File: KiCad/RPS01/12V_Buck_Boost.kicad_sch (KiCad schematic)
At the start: 0 parts

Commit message: Updfates
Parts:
- added C(STBYMD)1, Css1: 0.001u, Capacitor_SMD:C_1206_3216Metric, symbol Device:C
- added C(lowESR)1: 4.7u, Mechatronic Footprints:LOWESRCAPMP7.6X4.3_3.1N_KEM, symbol Device:C
- added Ca(SW1)1, Cb(SW2)1: 0.22u, Capacitor_SMD:C_1206_3216Metric, symbol Device:C
- added Cb(out)1: 330u, Mechatronic Footprints:LargeCAPSCAPPRD350W60D800H1200, symbol Device:C_Polarized
- added Cc(out)1: 47u, Capacitor_SMD:C_1206_3216Metric, symbol Device:C
- added Cin(b)1: 270u, Mechatronic Footprints:LargeCAPSCAPPRD350W60D800H1200, symbol Device:C
- added Cin(c)1: 10u, Capacitor_SMD:C_1206_3216Metric, symbol Device:C
- added Cout(filter)1: 330u, Mechatronic Footprints:LargeCAPSCAPPRD350W60D800H1200, symbol Device:C
- added Cs1: 100p, Capacitor_SMD:C_1206_3216Metric, symbol Device:C
- added Cth1: 10000p, Capacitor_SMD:C_1206_3216Metric, symbol Device:C
- added Cthp1: 47p, Capacitor_SMD:C_1206_3216Metric, symbol Device:C
- added D(Zener)2: D_Zener, Mechatronic Footprints:SOD123_DIO, symbol Device:D_Zener
- added D1, D2, D4, D5: D_Schottky, Mechatronic Footprints:CR_SMA_320-340AE_DIO, symbol Device:D_Schottky
- added L1: 6.8u, Mechatronic Footprints:IND_410680_WRE, symbol Device:L
- added Q1, Q2, Q3, Q4: NMOS, Mechatronic Footprints:Q1Q2TRANS_FDMC86520L, symbol Device:Q_NMOS_DGS
- added R(pgood)1: 100k, LED_SMD:LED_1206_3216Metric, symbol Device:R
- added R4, R5: 100, Resistor_SMD:R_1206_3216Metric, symbol Device:R
- added Rb1: 4.3K, Resistor_SMD:R_1206_3216Metric, symbol Device:R
- added Rin(Run)1: 51K, Resistor_SMD:R_1206_3216Metric, symbol Device:R
- added Rs1, Rsen1: 6m, Resistor_SMD:R_2512_6332Metric, symbol Device:R
- added Rt1: 100K, Resistor_SMD:R_1206_3216Metric, symbol Device:R
- added Rth1: 124K, Resistor_SMD:R_1206_3216Metric, symbol Device:R
- added U1: LTC3780EG-TRPBF, LTC3780:SSOP-24_G_LIT, symbol LTC3780-24-SSOP:LTC3780EG-TRPBF
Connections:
- new net: C(lowESR)1.1, D4.2 (A), D5.2 (A), R(pgood)1.1, U1.19 (INTVCC)
- new net: R(pgood)1.2, U1.1 (PGOOD)
- new net: Ca(SW1)1.2, D1.2 (A), L1.2, Q3.3 (S), Q4.1 (D), U1.22 (SW1)
- new net: Q4.2 (G), U1.18 (BG1)
- new net: D2.2 (A), Q2.3 (S), Q4.3 (S), R4.1, Rs1.1, Rsen1.1
- new net: C(STBYMD)1.1, U1.12 (STBYMD)
- new net: Cb(SW2)1.2, D5.1 (K), U1.13 (BOOST2)
- new net: Q1.2 (G), U1.14 (TG2)
- new net: Cb(SW2)1.1, D2.1 (K), L1.1, Q1.3 (S), Q2.1 (D), U1.15 (SW2)
- new net: Q2.2 (G), U1.16 (BG2)
- new net: Css1.2, U1.2 (SS)
- new net: Q3.2 (G), U1.23 (TG1)
- new net: Ca(SW1)1.1, D4.1 (K), U1.24 (BOOST1)
- new net: Cs1.2, R4.2, U1.3 (SENSE+)
- new net: Cs1.1, R5.1, U1.4 (SENSE-)
- new net: Cthp1.1, Rth1.2, U1.5 (ITH)
- new net: Rb1.1, Rt1.2, U1.6 (VOSENSE)
- new net: D(Zener)2.1 (K), Rin(Run)1.2, U1.8 (RUN)
- new net: Cth1.1, Rth1.1
- new net GND: C(STBYMD)1.2, C(lowESR)1.2, Cb(out)1.2, Cc(out)1.2, Cin(b)1.2, Cin(c)1.2, Cout(filter)1.2, Css1.1, Cth1.2, Cthp1.2, D(Zener)2.2 (A), R5.2, Rb1.2, Rs1.2, Rsen1.2, U1.10 (PLLFLTR), U1.17 (PGND), U1.20 (EXTVCC), U1.7 (SGND), U1.9 (FCB)
- new net Vin: Cin(b)1.1, Cin(c)1.1, Q1.1 (D), Rin(Run)1.1, U1.21 (VIN)
- new net Vout: Cb(out)1.1, Cc(out)1.1, Cout(filter)1.1, D1.1 (K), Q3.1 (D), Rt1.1
- no-connect marks 0 -> 1

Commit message: Changed footprints on my end only
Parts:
- U1: footprint LTC3780:SSOP-24_G_LIT -> Mechatronics LTC3780:SSOP-24_G_LIT
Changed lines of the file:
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@@
       (effects (font (size 1.524 1.524)))
     )
-    (property "Footprint" "LTC3780:SSOP-24_G_LIT" (at 111.0742 89.4334 0)
+    (property "Footprint" "Mechatronics LTC3780:SSOP-24_G_LIT" (at 111.0742 89.4334 0)
       (effects (font (size 1.27 1.27) italic) hide)
     )

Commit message: All Footprints Load from Mechatronics Folder
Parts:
- U1: footprint Mechatronics LTC3780:SSOP-24_G_LIT -> Mechatronic Footprints:LTC3780_SSOP-24_G_LIT
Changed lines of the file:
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@@
       (effects (font (size 1.524 1.524)))
     )
-    (property "Footprint" "Mechatronics LTC3780:SSOP-24_G_LIT" (at 111.0742 89.4334 0)
+    (property "Footprint" "Mechatronic Footprints:LTC3780_SSOP-24_G_LIT" (at 111.0742 89.4334 0)
       (effects (font (size 1.27 1.27) italic) hide)
     )

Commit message: Deleted 12 and 5 V. 19V updated
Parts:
- removed C(STBYMD)1, Css1: 0.001u, Capacitor_SMD:C_1206_3216Metric, symbol Device:C
- removed C(lowESR)1: 4.7u, Mechatronic Footprints:LOWESRCAPMP7.6X4.3_3.1N_KEM, symbol Device:C
- removed Ca(SW1)1, Cb(SW2)1: 0.22u, Capacitor_SMD:C_1206_3216Metric, symbol Device:C
- removed Cb(out)1: 330u, Mechatronic Footprints:LargeCAPSCAPPRD350W60D800H1200, symbol Device:C_Polarized
- removed Cc(out)1: 47u, Capacitor_SMD:C_1206_3216Metric, symbol Device:C
- removed Cin(b)1: 270u, Mechatronic Footprints:LargeCAPSCAPPRD350W60D800H1200, symbol Device:C
- removed Cin(c)1: 10u, Capacitor_SMD:C_1206_3216Metric, symbol Device:C
- removed Cout(filter)1: 330u, Mechatronic Footprints:LargeCAPSCAPPRD350W60D800H1200, symbol Device:C
- removed Cs1: 100p, Capacitor_SMD:C_1206_3216Metric, symbol Device:C
- removed Cth1: 10000p, Capacitor_SMD:C_1206_3216Metric, symbol Device:C
- removed Cthp1: 47p, Capacitor_SMD:C_1206_3216Metric, symbol Device:C
- removed D(Zener)2: D_Zener, Mechatronic Footprints:SOD123_DIO, symbol Device:D_Zener
- removed D1, D2, D4, D5: D_Schottky, Mechatronic Footprints:CR_SMA_320-340AE_DIO, symbol Device:D_Schottky
- removed L1: 6.8u, Mechatronic Footprints:IND_410680_WRE, symbol Device:L
- removed Q1, Q2, Q3, Q4: NMOS, Mechatronic Footprints:Q1Q2TRANS_FDMC86520L, symbol Device:Q_NMOS_DGS
- removed R(pgood)1: 100k, LED_SMD:LED_1206_3216Metric, symbol Device:R
- removed R4, R5: 100, Resistor_SMD:R_1206_3216Metric, symbol Device:R
- removed Rb1: 4.3K, Resistor_SMD:R_1206_3216Metric, symbol Device:R
- removed Rin(Run)1: 51K, Resistor_SMD:R_1206_3216Metric, symbol Device:R
- removed Rs1, Rsen1: 6m, Resistor_SMD:R_2512_6332Metric, symbol Device:R
- removed Rt1: 100K, Resistor_SMD:R_1206_3216Metric, symbol Device:R
- removed Rth1: 124K, Resistor_SMD:R_1206_3216Metric, symbol Device:R
- removed U1: LTC3780EG-TRPBF, Mechatronic Footprints:LTC3780_SSOP-24_G_LIT, symbol LTC3780-24-SSOP:LTC3780EG-TRPBF
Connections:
- no-connect marks 1 -> 0

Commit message: Added prototype 12V and 5V boards
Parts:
- added C(STBYMD)1, Css1: 0.001u, Capacitor_SMD:C_1206_3216Metric, symbol Device:C
- added C(lowESR)1: 4.7u, Mechatronics Cesr:CAPMP7.6X4.3_3.1N_KEM, symbol Device:C
- added Ca(SW1)1, Cb(SW2)1: 0.22u, Capacitor_SMD:C_1206_3216Metric, symbol Device:C
- added Cc(out)1: 47u, Capacitor_SMD:C_1206_3216Metric, symbol Device:C
- added Cin(b)1: 270u, Mechatronic Footprints:LargeCAPSCAPPRD350W60D800H1200, symbol Device:C
- added Cin(c)1: 10u, Capacitor_SMD:C_1206_3216Metric, symbol Device:C
- added Cout_19V_EEH-ZU1V331P1: 330u, Mechatronic Footprints:LargeCAPSCAPPRD350W60D800H1200, symbol Device:C
- added Cout_b_19V_EEH-ZU1V331P1: 330u, Mechatronic Footprints:LargeCAPSCAPPRD350W60D800H1200, symbol Device:C_Polarized
- added Cs1: 100p, Capacitor_SMD:C_1206_3216Metric, symbol Device:C
- added Cth1: 10000p, Capacitor_SMD:C_1206_3216Metric, symbol Device:C
- added Cthp1: 47p, Capacitor_SMD:C_1206_3216Metric, symbol Device:C
- added D(Zener)_19V1: D_Zener_BZT52C4V7-13-F, Mechatronic Footprints:SOD123_DIO, symbol Device:D_Zener
- added D1(2)_19V1, D2(1)_19V1: SD2114S040S8R0, Mechatronics Sdiode:SD2114_AVX, symbol Mechatronics Sdiode:SD2114S040S8R0
- added D4_19V1, D5_19V1: D_Schottky_B340AE-13, Mechatronic Footprints:CR_SMA_320-340AE_DIO, symbol Device:D_Schottky
- added L1_19V1: 6.8u Wurth 74436410680, Mechatronic Footprints:IND_410680_WRE, symbol Device:L
- added QA(1)_19V_2, QB(2)_19V_1, QC(4)_19V_1, QD(3)_19V_3: BSC009NE2LS5IATMA1, Mechatronic Footprints:PG-TDSON-8_INF_modified_ken, symbol Mechatronics NMOS:BSC009NE2LS5IATMA1
- added R(pgood)1: 100k, LED_SMD:LED_1206_3216Metric, symbol Device:R
- added R4, R5: 100, Resistor_SMD:R_1206_3216Metric, symbol Device:R
- added Rb1: 4.3K, Resistor_SMD:R_1206_3216Metric, symbol Device:R
- added Rin(Run)1: 51K, Resistor_SMD:R_1206_3216Metric, symbol Device:R
- added Rs1, Rsen1: 6m, Resistor_SMD:R_2512_6332Metric, symbol Device:R
- added Rt1: 100K, Resistor_SMD:R_1206_3216Metric, symbol Device:R
- added Rth1: 124K, Resistor_SMD:R_1206_3216Metric, symbol Device:R
- added U1: LTC3780EG-TRPBF, Mechatronic Footprints:LTC3780_SSOP-24_G_LIT, symbol LTC3780-24-SSOP:LTC3780EG-TRPBF
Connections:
- new net GND: C(STBYMD)1.2, C(lowESR)1.2, Cc(out)1.2, Cin(b)1.2, Cin(c)1.2, Cout_19V_EEH-ZU1V331P1.2, Cout_b_19V_EEH-ZU1V331P1.2, Css1.1, Cth1.2, Cthp1.2, D(Zener)_19V1.2 (A), R5.2, Rb1.2, Rs1.2, Rsen1.2, U1.10 (PLLFLTR), U1.17 (PGND), U1.20 (EXTVCC), U1.7 (SGND), U1.9 (FCB)
- new net Net-(Cth2-Pad1): Cth1.1, Rth1.1
- new net Net-(D(Zener)_19V2-K): D(Zener)_19V1.1 (K), Rin(Run)1.2, U1.8 (RUN)
- new net Net-(D1(2)_19V2-Pad2): D1(2)_19V1.2, QB(2)_19V_1.1, QB(2)_19V_1.2, QB(2)_19V_1.3, QC(4)_19V_1.1, QC(4)_19V_1.2, QC(4)_19V_1.3, R4.1, Rs1.1, Rsen1.1
- new net Net-(D4_19V2-A): C(lowESR)1.1, D4_19V1.2 (A), D5_19V1.2 (A), R(pgood)1.1, U1.19 (INTVCC)
- new net Net-(D4_19V2-K): Ca(SW1)1.1, D4_19V1.1 (K), U1.24 (BOOST1)
- new net Net-(D5_19V2-K): Cb(SW2)1.2, D5_19V1.1 (K), U1.13 (BOOST2)
- new net Net-(U7-BG1): QC(4)_19V_1.4, U1.18 (BG1)
- new net Net-(U7-BG2): QB(2)_19V_1.4, U1.16 (BG2)
- new net Net-(U7-ITH): Cthp1.1, Rth1.2, U1.5 (ITH)
- new net Net-(U7-PGOOD): R(pgood)1.2, U1.1 (PGOOD)
- new net Net-(U7-SENSE+): Cs1.2, R4.2, U1.3 (SENSE+)
- new net Net-(U7-SENSE-): Cs1.1, R5.1, U1.4 (SENSE-)
- new net Net-(U7-SS): Css1.2, U1.2 (SS)
- new net Net-(U7-STBYMD): C(STBYMD)1.1, U1.12 (STBYMD)
- new net Net-(U7-SW1): Ca(SW1)1.2, D2(1)_19V1.2, L1_19V1.2, QC(4)_19V_1.5, QC(4)_19V_1.6, QC(4)_19V_1.7, QC(4)_19V_1.8, QD(3)_19V_3.1, QD(3)_19V_3.2, QD(3)_19V_3.3, U1.22 (SW1)
- new net Net-(U7-SW2): Cb(SW2)1.1, D1(2)_19V1.1, L1_19V1.1, QA(1)_19V_2.1, QA(1)_19V_2.2, QA(1)_19V_2.3, QB(2)_19V_1.5, QB(2)_19V_1.6, QB(2)_19V_1.7, QB(2)_19V_1.8, U1.15 (SW2)
- new net Net-(U7-TG1): QD(3)_19V_3.4, U1.23 (TG1)
- new net Net-(U7-TG2): QA(1)_19V_2.4, U1.14 (TG2)
- new net Net-(U7-VOSENSE): Rb1.1, Rt1.2, U1.6 (VOSENSE)
- new net Vin: Cin(b)1.1, Cin(c)1.1, QA(1)_19V_2.5, QA(1)_19V_2.6, QA(1)_19V_2.7, QA(1)_19V_2.8, Rin(Run)1.1, U1.21 (VIN)
- new net Vout: Cc(out)1.1, Cout_19V_EEH-ZU1V331P1.1, Cout_b_19V_EEH-ZU1V331P1.1, D2(1)_19V1.1, QD(3)_19V_3.5, QD(3)_19V_3.6, QD(3)_19V_3.7, QD(3)_19V_3.8, Rt1.1
- new net unconnected-(U7-PLLIN-Pad11): U1.11 (PLLIN)
- no-connect marks 0 -> 2

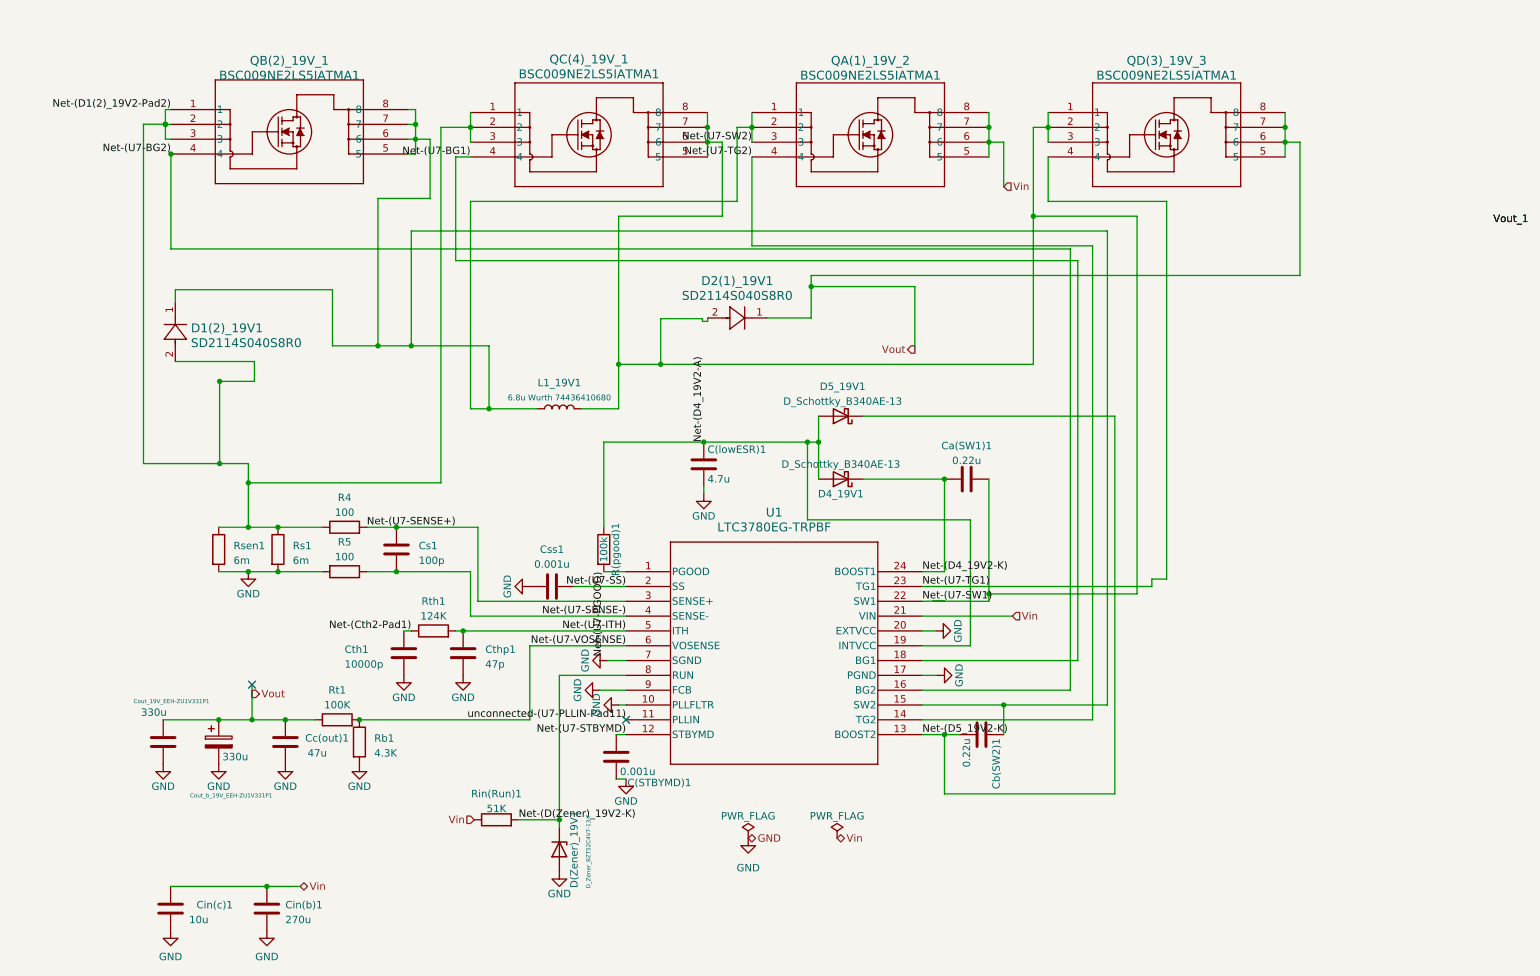
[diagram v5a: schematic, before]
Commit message: Fixing 5V Problems
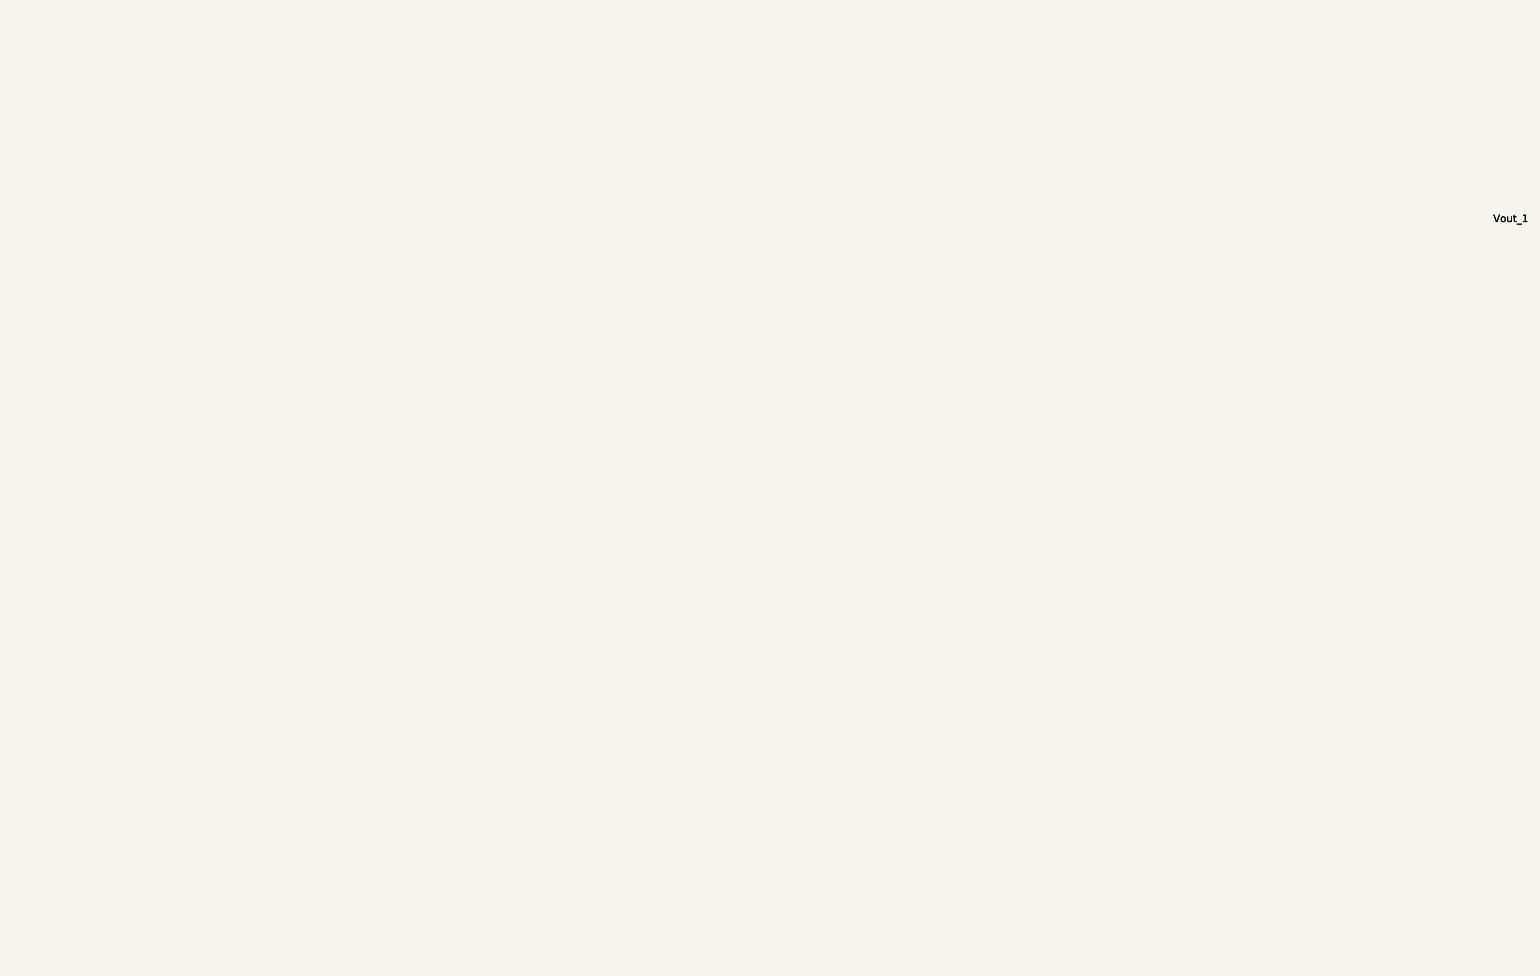
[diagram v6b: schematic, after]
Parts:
- removed C(STBYMD)1, Css1: 0.001u, Capacitor_SMD:C_1206_3216Metric, symbol Device:C
- removed C(lowESR)1: 4.7u, Mechatronics Cesr:CAPMP7.6X4.3_3.1N_KEM, symbol Device:C
- removed Ca(SW1)1, Cb(SW2)1: 0.22u, Capacitor_SMD:C_1206_3216Metric, symbol Device:C
- removed Cc(out)1: 47u, Capacitor_SMD:C_1206_3216Metric, symbol Device:C
- removed Cin(b)1: 270u, Mechatronic Footprints:LargeCAPSCAPPRD350W60D800H1200, symbol Device:C
- removed Cin(c)1: 10u, Capacitor_SMD:C_1206_3216Metric, symbol Device:C
- removed Cout_19V_EEH-ZU1V331P1: 330u, Mechatronic Footprints:LargeCAPSCAPPRD350W60D800H1200, symbol Device:C
- removed Cout_b_19V_EEH-ZU1V331P1: 330u, Mechatronic Footprints:LargeCAPSCAPPRD350W60D800H1200, symbol Device:C_Polarized
- removed Cs1: 100p, Capacitor_SMD:C_1206_3216Metric, symbol Device:C
- removed Cth1: 10000p, Capacitor_SMD:C_1206_3216Metric, symbol Device:C
- removed Cthp1: 47p, Capacitor_SMD:C_1206_3216Metric, symbol Device:C
- removed D(Zener)_19V1: D_Zener_BZT52C4V7-13-F, Mechatronic Footprints:SOD123_DIO, symbol Device:D_Zener
- removed D1(2)_19V1, D2(1)_19V1: SD2114S040S8R0, Mechatronics Sdiode:SD2114_AVX, symbol Mechatronics Sdiode:SD2114S040S8R0
- removed D4_19V1, D5_19V1: D_Schottky_B340AE-13, Mechatronic Footprints:CR_SMA_320-340AE_DIO, symbol Device:D_Schottky
- removed L1_19V1: 6.8u Wurth 74436410680, Mechatronic Footprints:IND_410680_WRE, symbol Device:L
- removed QA(1)_19V_2, QB(2)_19V_1, QC(4)_19V_1, QD(3)_19V_3: BSC009NE2LS5IATMA1, Mechatronic Footprints:PG-TDSON-8_INF_modified_ken, symbol Mechatronics NMOS:BSC009NE2LS5IATMA1
- removed R(pgood)1: 100k, LED_SMD:LED_1206_3216Metric, symbol Device:R
- removed R4, R5: 100, Resistor_SMD:R_1206_3216Metric, symbol Device:R
- removed Rb1: 4.3K, Resistor_SMD:R_1206_3216Metric, symbol Device:R
- removed Rin(Run)1: 51K, Resistor_SMD:R_1206_3216Metric, symbol Device:R
- removed Rs1, Rsen1: 6m, Resistor_SMD:R_2512_6332Metric, symbol Device:R
- removed Rt1: 100K, Resistor_SMD:R_1206_3216Metric, symbol Device:R
- removed Rth1: 124K, Resistor_SMD:R_1206_3216Metric, symbol Device:R
- removed U1: LTC3780EG-TRPBF, Mechatronic Footprints:LTC3780_SSOP-24_G_LIT, symbol LTC3780-24-SSOP:LTC3780EG-TRPBF
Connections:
- no-connect marks 2 -> 0
